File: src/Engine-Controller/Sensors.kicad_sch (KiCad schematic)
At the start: 0 parts

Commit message: added pt connectors to schematic
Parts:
- added P? (x8): 39299043, CONN_4840.2201_SCH, symbol Engine-Controller:39299043
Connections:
- new net 3.3V: P?.1 (+12V), P?.1 (+12V), P?.1 (+12V), P?.1 (+12V), P?.1 (+12V), P?.1 (+12V), P?.1 (+12V), P?.1 (+12V)
- new net Earth: P?.4, P?.4, P?.4, P?.4, P?.4, P?.4, P?.4, P?.4
- new net PT1+: P?.2 (GND)
- new net PT1-: P?.3
- new net PT2+: P?.2 (GND)
- new net PT2-: P?.3
- new net PT3+: P?.2 (GND)
- new net PT3-: P?.3
- new net PT4+: P?.2 (GND)
- new net PT4-: P?.3
- new net PT5+: P?.2 (GND)
- new net PT5-: P?.3
- new net PT6+: P?.2 (GND)
- new net PT6-: P?.3
- new net PT7+: P?.2 (GND)
- new net PT7-: P?.3
- new net PT8+: P?.2 (GND)
- new net PT8-: P?.3

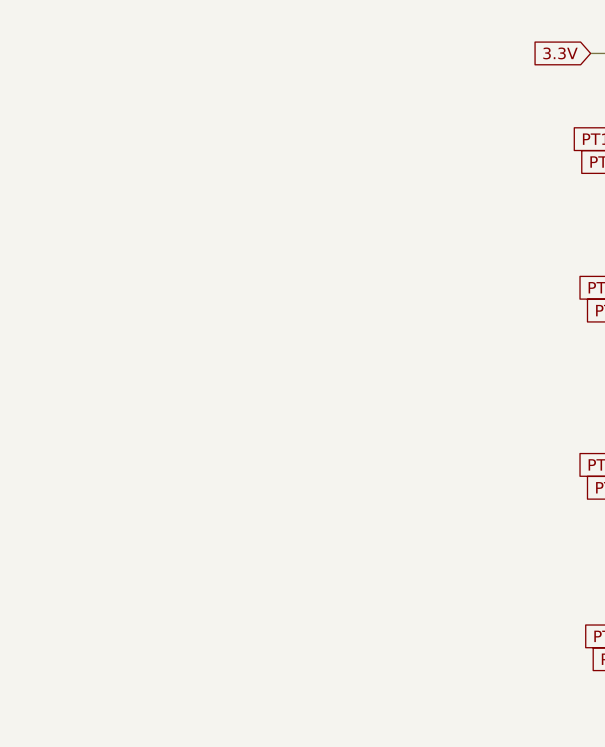
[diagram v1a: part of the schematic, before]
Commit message: added pt multiplexors to schematic
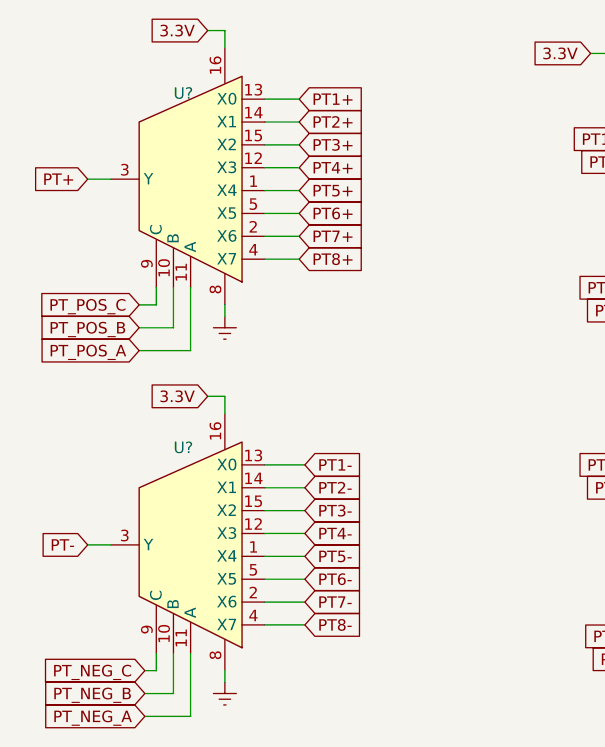
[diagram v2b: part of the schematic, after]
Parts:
- added U? (x2): MAX4617EUE+T, symbol Engine-Controller:MAX4617EUE+T
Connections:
- net 3.3V: now also U?.16, U?.16
- net Earth: now also U?.8, U?.8
- net PT1+: now also U?.13 (X0)
- net PT1-: now also U?.13 (X0)
- net PT2+: now also U?.14 (X1)
- net PT2-: now also U?.14 (X1)
- net PT3+: now also U?.15 (X2)
- net PT3-: now also U?.15 (X2)
- net PT4+: now also U?.12 (X3)
- net PT4-: now also U?.12 (X3)
- net PT5+: now also U?.1 (X4)
- net PT5-: now also U?.1 (X4)
- net PT6+: now also U?.5 (X5)
- net PT6-: now also U?.5 (X5)
- net PT7+: now also U?.2 (X6)
- net PT7-: now also U?.2 (X6)
- net PT8+: now also U?.4 (X7)
- net PT8-: now also U?.4 (X7)
- new net PT+: U?.3 (Y)
- new net PT-: U?.3 (Y)
- new net PT_NEG_A: U?.11 (A)
- new net PT_NEG_B: U?.10 (B)
- new net PT_NEG_C: U?.9 (C)
- new net PT_POS_A: U?.11 (A)
- new net PT_POS_B: U?.10 (B)
- new net PT_POS_C: U?.9 (C)

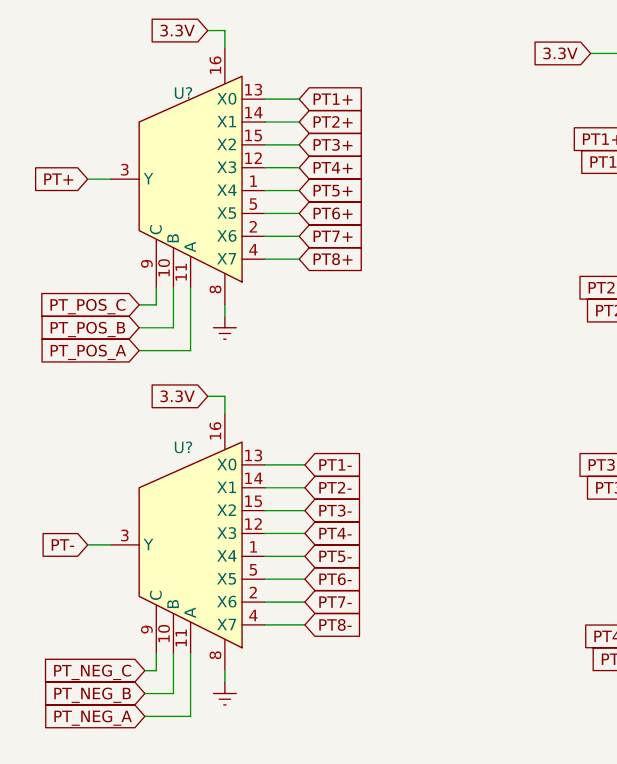
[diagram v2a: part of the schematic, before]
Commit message: added decoder footprint to lib files
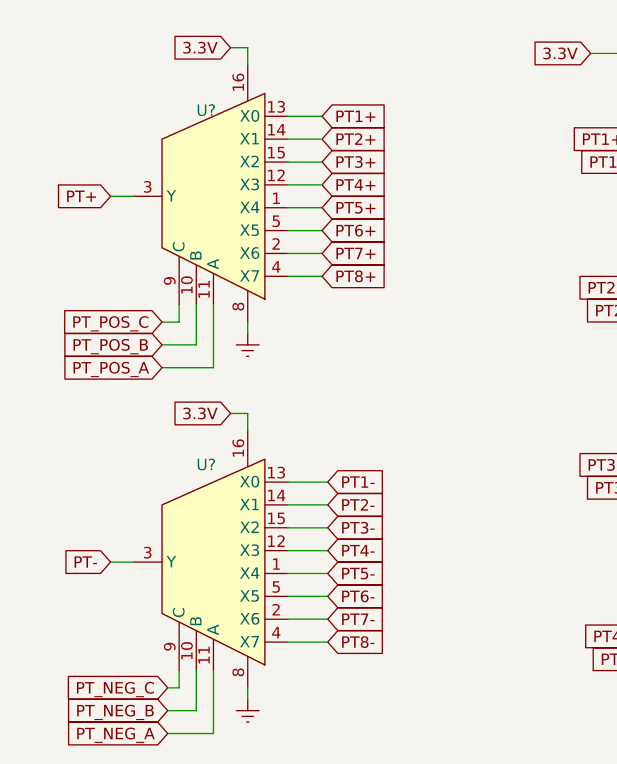
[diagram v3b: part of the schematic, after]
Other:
- moved on the sheet: U?

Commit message: finished pt schematic
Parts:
- added R? (x8): 1k, symbol Engine-Controller:RES_0603
- added U? (x10): MC74HC4066ADG, symbol Engine-Controller:MC74HC4066ADG
- added U?: AD623ARZ-R7, R_8_ADI, symbol Engine-Controller:AD623ARZ-R7
- added U?: CD74HC238M, symbol Engine-Controller:CD74HC238M
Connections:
- net 3.3V: now also U?.14, U?.14, U?.16 (VDD)
- net Earth: now also U?.4 (-VS), U?.4 (G0), U?.5 (G1), U?.5 (REF), U?.7, U?.7, U?.8 (GND)
- net PT+: now also U?.3 (+IN)
- net PT-: now also U?.2 (-IN)
- new net: U?.1, U?.1, U?.1 (-RG), U?.11, U?.11, U?.4, U?.4, U?.8, U?.8
- new net: R?.1, U?.2 (x2)
- new net: R?.1, U?.3 (x2)
- new net: R?.2, R?.2, R?.2, R?.2, R?.2, R?.2, R?.2, R?.2, U?.8 (+RG)
- new net: R?.1, U?.10 (x2)
- new net: R?.1, U?.9 (x2)
- new net 3.V: U?.6 (G2)
- new net 5V: U?.7 (+VS)
- new net PT: U?.6 (OUT)
- new net PT_GAIN0: U?.13, U?.15 (Y0)
- new net PT_GAIN1: U?.14 (Y1), U?.5
- new net PT_GAIN2: U?.13 (Y2), U?.6
- new net PT_GAIN3: U?.12, U?.12 (Y3)
- new net PT_GAIN4: U?.11 (Y4), U?.13
- new net PT_GAIN5: U?.10 (Y5), U?.5
- new net PT_GAIN6: U?.6, U?.9 (Y6)
- new net PT_GAIN7: U?.12, U?.7 (Y7)
- new net PT_GAIN_A0: U?.1 (A0)
- new net PT_GAIN_A1: U?.2 (A1)
- new net PT_GAIN_A2: U?.3 (A2)
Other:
- note added: "Analog Switch Power Supply"
- note added: "PT Analog Multiplexers"
- note added: "PT Gain Decoder"
- note added: "PT Programmable Gain Differential Amplifier"
- note added: "Pressure Transducer Connectors"
- moved on the sheet: P?, U?

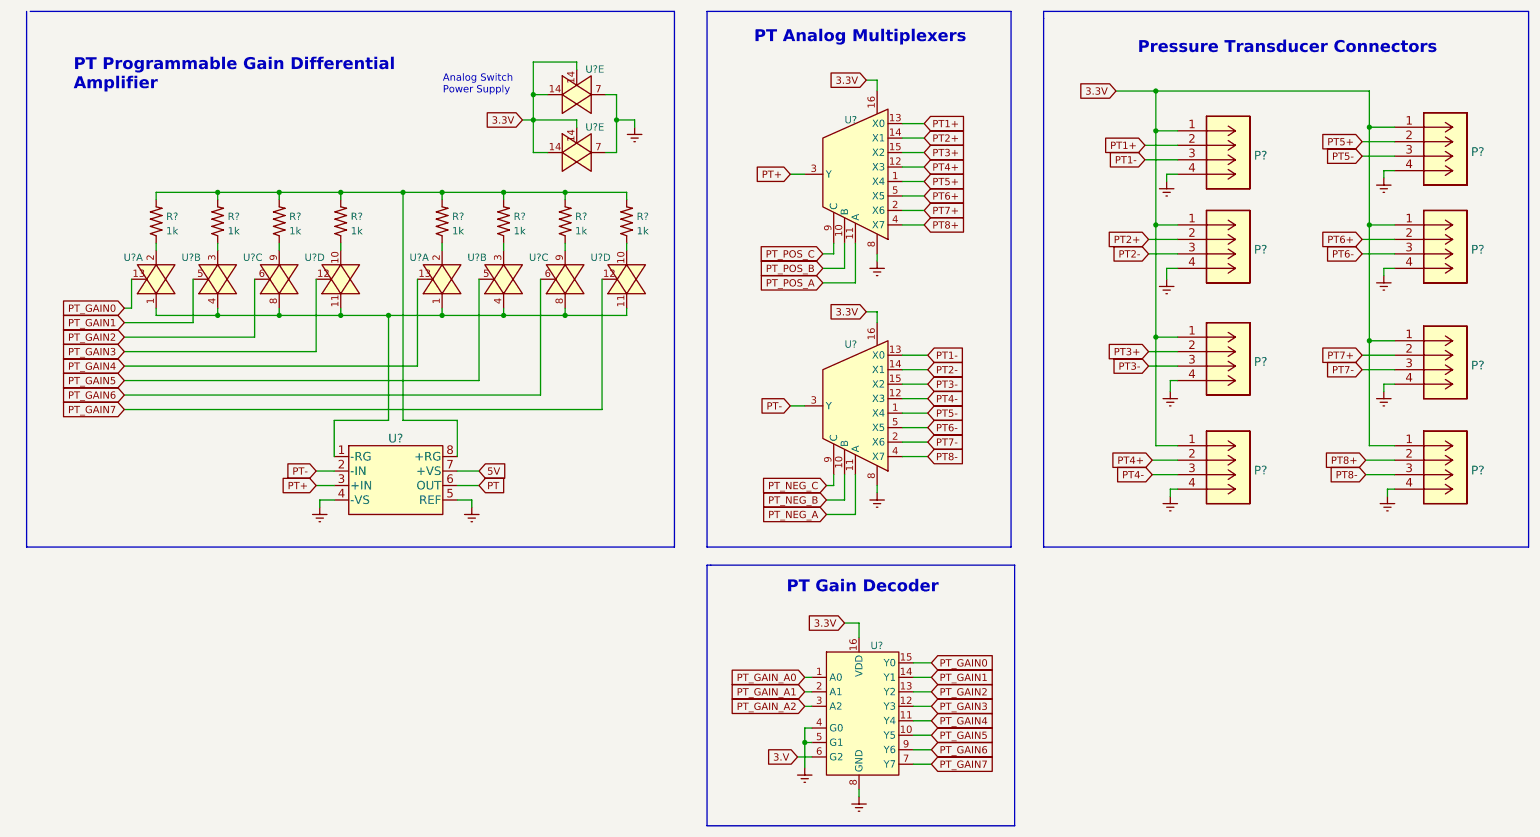
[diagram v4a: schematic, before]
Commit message: moved schematic components to 25 mil grid
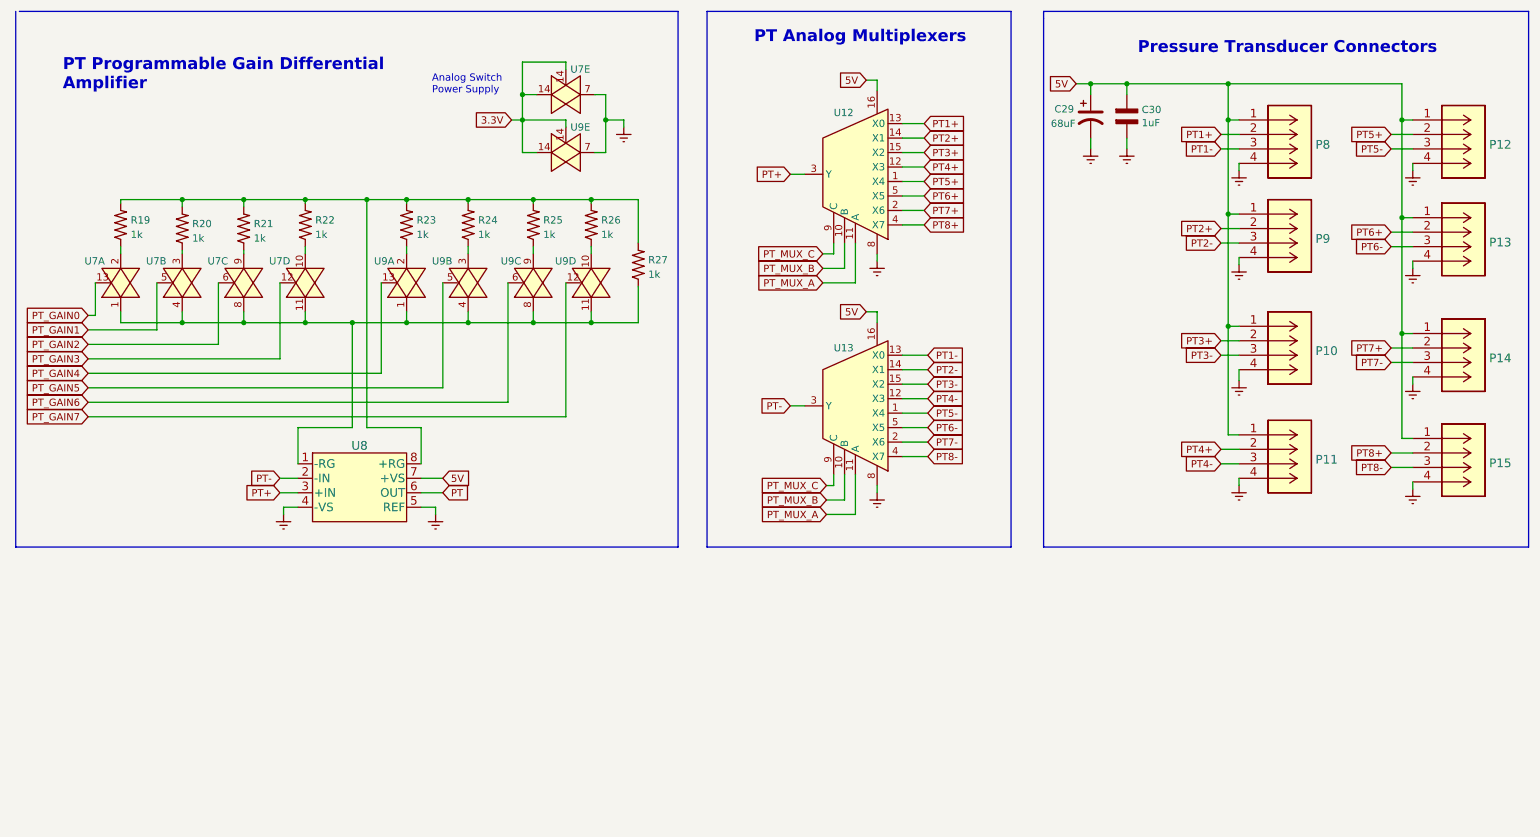
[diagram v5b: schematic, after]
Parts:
- removed U? (x10): MC74HC4066ADG, symbol Engine-Controller:MC74HC4066ADG
- removed U?: CD74HC238M, symbol Engine-Controller:CD74HC238M
- added C29: 68uF, Engine-Controller:EEEFPV680XAP, symbol Engine-Controller:UKL1C220KDDANATD
- added C30: 1uF, Engine-Controller:CAP_0603, symbol Engine-Controller:CAP_0603
- added R27: 1k, symbol Engine-Controller:RES_0603
- added U7, U9: MC74HC4066ADG, symbol Engine-Controller:MC74HC4066ADG
- gave numbers to parts that had none: 19
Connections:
- net PT_POS_A is gone; now on net PT_MUX_A: U12.11 (A)
- net PT_POS_B is gone; now on net PT_MUX_B: U12.10 (B)
- net PT_POS_C is gone; now on net PT_MUX_C: U12.9 (C)
- net 3.3V: now also U7.14, U9.14; no longer P10.1 (+12V), P11.1 (+12V), P12.1 (+12V), P13.1 (+12V), P14.1 (+12V), P15.1 (+12V), P8.1 (+12V), P9.1 (+12V), U12.16, U13.16
- net 5V: now also P10.1 (+12V), P11.1 (+12V), P12.1 (+12V), P13.1 (+12V), P14.1 (+12V), P15.1 (+12V), P8.1 (+12V), P9.1 (+12V), U12.16, U13.16, C29.1, C30.2
- net Earth: now also C29.2, C30.1, U7.7, U9.7
- net PT_GAIN0: now also U7.13
- net PT_GAIN1: now also U7.5
- net PT_GAIN2: now also U7.6
- net PT_GAIN3: now also U7.12
- net PT_GAIN4: now also U9.13
- net PT_GAIN5: now also U9.5
- net PT_GAIN6: now also U9.6
- net PT_GAIN7: now also U9.12
- net at U8.1 (-RG): now also R27.1, U7.1, U7.11, U7.4, U7.8, U9.1, U9.11, U9.4, U9.8
- net at R19.1: now also U7.2
- net at R20.1: now also U7.3
- net at R19.2, R20.2, R21.2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: now also R27.2
- net at R26.1: now also U9.10
- net at R25.1: now also U9.9
- net at R23.1: now also U9.2
- net at R24.1: now also U9.3
- net at R22.1: now also U7.10
- net at R21.1: now also U7.9
- net PT_NEG_A renamed PT_MUX_A
- net PT_NEG_B renamed PT_MUX_B
- net PT_NEG_C renamed PT_MUX_C
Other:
- note removed: "PT Gain Decoder"
- moved on the sheet: P10, P11, P12, P13, P14, P15, P8, P9, R19, R20, R21, R22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
